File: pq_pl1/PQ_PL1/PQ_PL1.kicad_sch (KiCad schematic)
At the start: 5 parts, among them J1 Conn_01x10, J2 Conn_01x10, J3 Conn_01x10, J4 Conn_01x10, J5 Conn_01x04

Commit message: Functional revision and finishing touches part II
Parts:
- removed J5: Conn_01x04, Connector_PinSocket_2.00mm:PinSocket_1x04_P2.00mm_Vertical, symbol Connector_Generic:Conn_01x04
- added H1, H2, H3, H4: MountingHole_Pad, MountingHole:MountingHole_3.2mm_M3_Pad, symbol Mechanical:MountingHole_Pad
- added U1: PTC06, sensor-nsl:PTC06, symbol sensor-nsl:PTC06
- J1: footprint Connector_PinSocket_2.54mm:PinSocket_1x10_P2.54mm_Vertical -> connector-nsl:SLW-110-01
- J2, J3, J4: footprint (none) -> connector-nsl:SLW-110-01
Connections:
- net MPPT_X is gone; now on net ADC_PL: J4.9 (Pin_9)
- net MPPT_Y is gone; now on net VCC_UMBILICAL: J3.8 (Pin_8)
- net MPPT_Z is gone; now on net FAULT: J3.9 (Pin_9)
- net RST_EPS is gone; now on net GND: J2.10 (Pin_10)
- net SEL_EPS is gone; now on net GND: J2.7 (Pin_7)
- net STM32_PA2 is gone; now on net SOLAR_X: J4.1 (Pin_1)
- net ADC_PH: now also J3.5 (Pin_5); no longer J3.6 (Pin_6)
- net ADC_PL: no longer J4.2 (Pin_2)
- net CHRG: now also J3.10 (Pin_10); no longer J3.1 (Pin_1)
- net CHRGOFF: now also J4.2 (Pin_2); no longer J4.7 (Pin_7)
- net CLPROG: now also J4.3 (Pin_3); no longer J4.8 (Pin_8)
- net DAC_PL: now also J4.8 (Pin_8); no longer J4.3 (Pin_3)
- net FAULT: no longer J3.2 (Pin_2)
- net GND: now also H1.1, H2.1, H3.1, H4.1, U1.1 (GND)
- net NRST: now also J4.5 (Pin_5); no longer J4.6 (Pin_6)
- net P/L_POWER: now also J3.6 (Pin_6); no longer J3.5 (Pin_5)
- net RST_DRIVERS: now also J3.4 (Pin_4); no longer J3.7 (Pin_7)
- net SEL_PH0: now also J3.7 (Pin_7); no longer J3.4 (Pin_4)
- net SOLAR_X: no longer J4.10 (Pin_10)
- net SOLAR_Z: now also J3.1 (Pin_1); no longer J3.10 (Pin_10)
- net SWCLK: now also J4.7 (Pin_7); no longer J4.4 (Pin_4)
- net SWDIO: now also J4.6 (Pin_6); no longer J4.5 (Pin_5)
- net UART_RX: now also U1.2 (RX)
- net UART_TX: now also U1.3 (TX)
- net VCC_UMBILICAL: no longer J3.3 (Pin_3)
- net HEATER_EN renamed HEATER_PWR
- net P/L2BURN renamed STM32_PA15
- net SCL renamed SCL1
- net SDA renamed SDA1
- net STM32_PD2 renamed BATT_NTC
- net TOTAL_CURRENT renamed NC
- net VCC renamed 3V3_PERM
- net 3V3_PERM: now also U1.4 (3V3)
- new net ADCS_POWER: J3.3 (Pin_3)
- new net SCL3: J4.10 (Pin_10)
- new net SDA3: J4.4 (Pin_4)
- new net STM32_PB0: J3.2 (Pin_2)
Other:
- note added: "Camera chip"
- note added: "MOUNTING HOLES"
- note added: "Vertical Connectors"
- moved on the sheet: J1, J2

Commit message: Full Kicad7 transition, library improvement and adaptation, correct footprints and 3D models added
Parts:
- J1, J2, J3, J4: footprint connector-nsl:SLW-110-01 -> -nsl_connector:BBL-110-Y-X
- U1: footprint sensor-nsl:PTC06 -> -nsl_sensor:PTC06; symbol sensor-nsl:PTC06 -> -nsl_sensor:PTC06

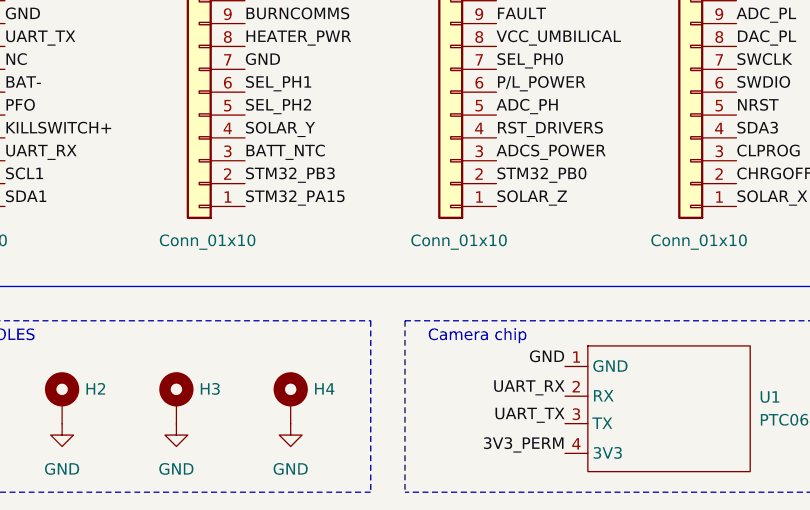
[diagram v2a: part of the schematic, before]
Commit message: J2(2) pin rename to SWO; DRC, fixed missconnection of VGA power to P/L_power pin instead of the generic 3V3_perm
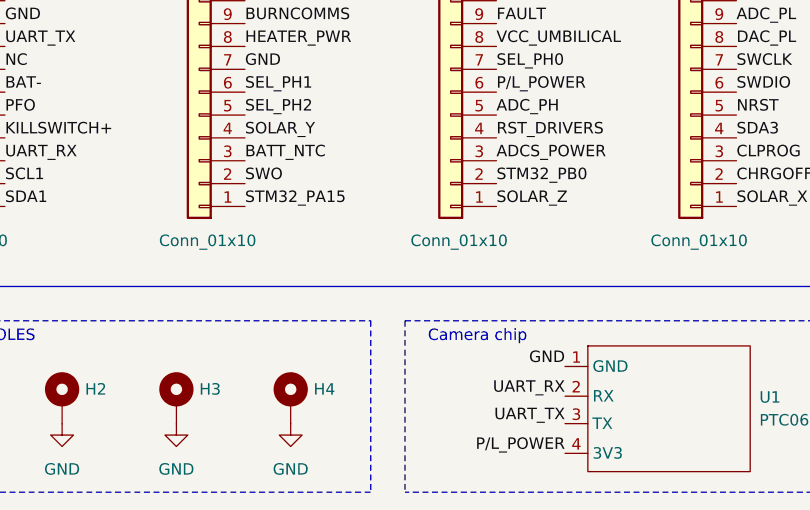
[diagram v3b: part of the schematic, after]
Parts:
- J1, J2, J3, J4: footprint -nsl_connector:BBL-110-Y-X -> connector-nsl:BBL-110-Y-X
- U1: footprint -nsl_sensor:PTC06 -> sensor-nsl:PTC06
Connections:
- net 3V3_PERM: no longer U1.4 (3V3)
- net P/L_POWER: now also U1.4 (3V3)
- net STM32_PB3 renamed SWO
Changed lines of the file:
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@@
     (effects (font (size 1.27 1.27)) (justify left bottom))
   )
-  (label "STM32_PB3" (at 99.06 81.28 0) (fields_autoplaced)
+  (label "SWO" (at 99.06 81.28 0) (fields_autoplaced)
     (effects (font (size 1.27 1.27)) (justify left bottom))
   )
@@
     (effects (font (size 1.27 1.27)) (justify left bottom))
   )
+  (label "P{slash}L_POWER" (at 134.62 111.252 180) (fields_autoplaced)
+    (effects (font (size 1.27 1.27)) (justify right bottom))
+  )
   (label "STM32_PB0" (at 127 81.28 0) (fields_autoplaced)
     (effects (font (size 1.27 1.27)) (justify left bottom))
@@
   (label "BAT-" (at 72.39 71.12 0) (fields_autoplaced)
     (effects (font (size 1.27 1.27)) (justify left bottom))
-  )
-  (label "3V3_PERM" (at 134.62 111.252 180) (fields_autoplaced)
-    (effects (font (size 1.27 1.27)) (justify right bottom))
   )
   (label "GND" (at 99.06 68.58 0) (fields_autoplaced)
@@
       (effects (font (size 1.27 1.27)))
     )
-    (property "Footprint" "-nsl_connector:BBL-110-Y-X" (at 67.31 73.66 0)
+    (property "Footprint" "connector-nsl:BBL-110-Y-X" (at 67.31 73.66 0)
       (effects (font (size 1.27 1.27)) hide)
     )
@@
       (effects (font (size 1.27 1.27)) (justify left))
     )
-    (property "Footprint" "-nsl_connector:BBL-110-Y-X" (at 121.92 73.66 0)
+    (property "Footprint" "connector-nsl:BBL-110-Y-X" (at 121.92 73.66 0)
       (effects (font (size 1.27 1.27)) hide)
     )
@@
       (effects (font (size 1.27 1.27)) (justify left))
     )
-    (property "Footprint" "-nsl_connector:BBL-110-Y-X" (at 148.59 73.66 0)
+    (property "Footprint" "connector-nsl:BBL-110-Y-X" (at 148.59 73.66 0)
       (effects (font (size 1.27 1.27)) hide)
     )
@@
       (effects (font (size 1.27 1.27)) (justify left))
     )
-    (property "Footprint" "-nsl_connector:BBL-110-Y-X" (at 93.98 73.66 0)
+    (property "Footprint" "connector-nsl:BBL-110-Y-X" (at 93.98 73.66 0)
       (effects (font (size 1.27 1.27)) hide)
     )
@@
       (effects (font (size 1.27 1.27)) (justify left))
     )
-    (property "Footprint" "-nsl_sensor:PTC06" (at 146.304 106.172 0)
-      (effects (font (size 1.27 1.27)) hide)
-    )
+    (property "Footprint" "sensor-nsl:PTC06" (at 146.304 106.172 0)
+      (effects (font (size 1.27 1.27)) hide)
+    )
